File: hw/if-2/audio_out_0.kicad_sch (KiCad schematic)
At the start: 18 parts, among them U4 TL072

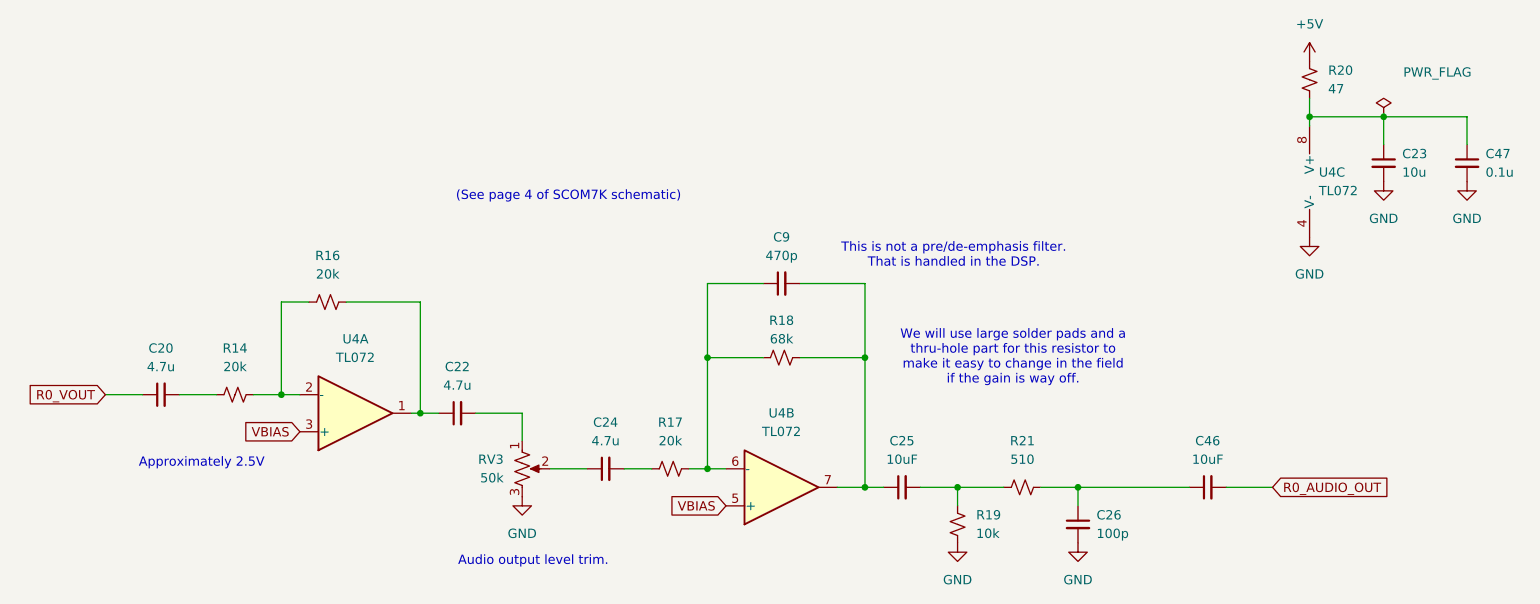
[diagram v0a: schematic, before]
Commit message: Ready to do layout on IF2 board
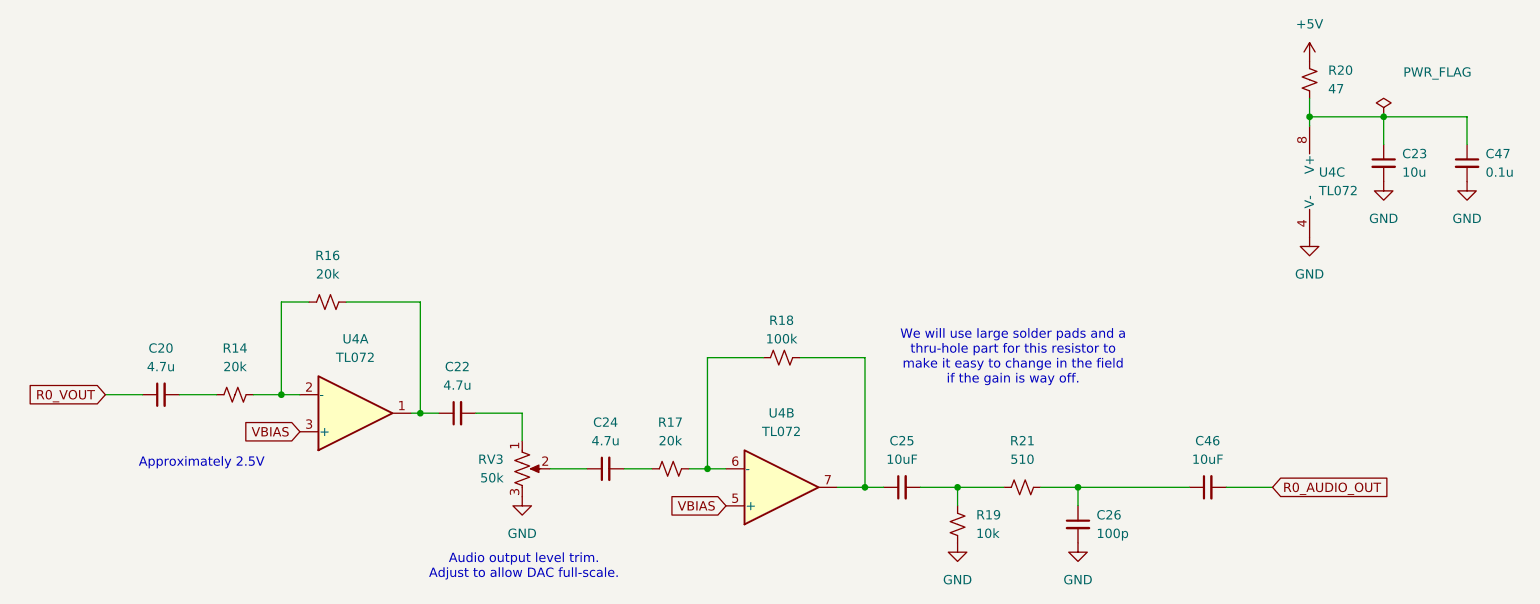
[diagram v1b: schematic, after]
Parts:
- removed C9: 470p, symbol Device:C_Small
- R18: value 68k -> 100k
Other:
- note added: "Audio output level trim. Adjust to allow DAC full-scale."
- note removed: "(See page 4 of SCOM7K schematic)"
- note removed: "Audio output level trim."
- note removed: "This is not a pre/de-emphasis filter. That is handled in the DSP."
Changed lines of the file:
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@@
 		)
 	)
-	(text "Audio output level trim.\n"
-		(exclude_from_sim no)
-		(at 122.174 96.52 0)
+	(text "Audio output level trim.\nAdjust to allow DAC full-scale.\n"
+		(exclude_from_sim no)
+		(at 120.904 97.282 0)
 		(effects
 			(font
 				(size 1.27 1.27)
-			)
-		)
-	)
-	(text "(See page 4 of SCOM7K schematic)"
-		(exclude_from_sim no)
-		(at 127 46.482 0)
-		(effects
-			(font
-				(size 1.27 1.27)
-			)
-		)
-	)
-	(text "This is not a pre/de-emphasis filter.\nThat is handled in the DSP."
-		(exclude_from_sim no)
-		(at 179.832 54.61 0)
-		(effects
-			(font
-				(size 1.27 1.27)
-				(color 255 4 2 1)
 			)
 		)
@@
 	)
 	(junction
-		(at 167.64 68.58)
-		(diameter 0)
-		(color 0 0 0 0)
-	)
-	(junction
 		(at 106.68 76.2)
 		(diameter 0)
@@
 	)
 	(junction
-		(at 146.05 68.58)
-		(diameter 0)
-		(color 0 0 0 0)
-	)
-	(junction
 		(at 238.76 35.56)
 		(diameter 0)
@@
 	(wire
 		(pts
-			(xy 167.64 58.42) (xy 167.64 68.58)
-		)
-		(stroke
-			(width 0)
-			(type default)
-		)
-	)
-	(wire
-		(pts
 			(xy 87.63 73.66) (xy 90.17 73.66)
 		)
@@
 	(wire
 		(pts
-			(xy 158.75 58.42) (xy 167.64 58.42)
-		)
-		(stroke
-			(width 0)
-			(type default)
-		)
-	)
-	(wire
-		(pts
 			(xy 228.6 35.56) (xy 228.6 36.83)
 		)
@@
 	(wire
 		(pts
-			(xy 146.05 58.42) (xy 146.05 68.58)
-		)
-		(stroke
-			(width 0)
-			(type default)
-		)
-	)
-	(wire
-		(pts
 			(xy 146.05 83.82) (xy 148.59 83.82)
 		)
@@
 		(pts
 			(xy 106.68 76.2) (xy 109.22 76.2)
-		)
-		(stroke
-			(width 0)
-			(type default)
-		)
-	)
-	(wire
-		(pts
-			(xy 153.67 58.42) (xy 146.05 58.42)
 		)
 		(stroke
@@
 	(symbol
 		(lib_id "Device:C_Small")
-		(at 156.21 58.42 90)
-		(unit 1)
-		(exclude_from_sim no)
-		(in_bom yes)
-		(on_board yes)
-		(dnp no)
-		(fields_autoplaced yes)
-		(property "Reference" "C9"
-			(at 156.2163 52.07 90)
-			(effects
-				(font
-					(size 1.27 1.27)
-				)
-			)
-		)
-		(property "Value" "470p"
-			(at 156.2163 54.61 90)
-			(effects
-				(font
-					(size 1.27 1.27)
-				)
-			)
-		)
-		(property "Footprint" ""
-			(at 156.21 58.42 0)
-			(effects
-				(font
-					(size 1.27 1.27)
-				)
-				(hide yes)
-			)
-		)
-		(property "Datasheet" "~"
-			(at 156.21 58.42 0)
-			(effects
-				(font
-					(size 1.27 1.27)
-				)
-				(hide yes)
-			)
-		)
-		(property "Description" "Unpolarized capacitor, small symbol"
-			(at 156.21 58.42 0)
-			(effects
-				(font
-					(size 1.27 1.27)
-				)
-				(hide yes)
-			)
-		)
-		(pin "1"
-		)
-		(pin "2"
-		)
-		(instances
-			(project ""
-				(path "/a8c2d6aa-29bb-49bd-a367-0d62a0a32480/44344ba6-1370-4a77-ab96-dbf60268a0b4"
-					(reference "C9")
-					(unit 1)
-				)
-			)
-		)
-	)
-	(symbol
-		(lib_id "Device:C_Small")
 		(at 172.72 86.36 90)
 		(unit 1)
@@
 			)
 		)
-		(property "Value" "68k"
+		(property "Value" "100k"
 			(at 156.21 66.04 90)
 			(effects

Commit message: Ready to do layout on IF2 board
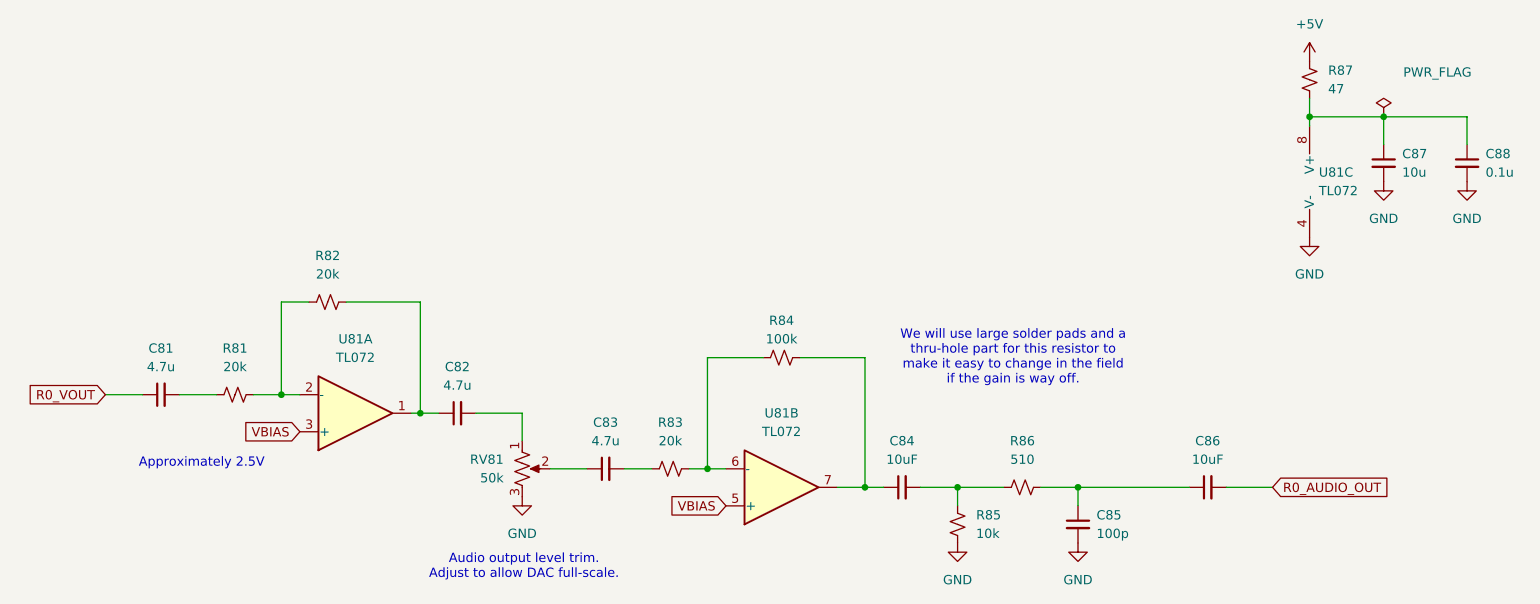
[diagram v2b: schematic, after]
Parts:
- R84: renamed from R18; footprint Resistor_SMD:R_0805_2012Metric_Pad1.20x1.40mm_HandSolder -> Resistor_THT:R_Axial_DIN0516_L15.5mm_D5.0mm_P5.08mm_Vertical
- U81: renamed from U4; footprint (none) -> Package_SO:SOIC-8_3.9x4.9mm_P1.27mm
- renumbered C20 to C81, C22 to C82, C24 to C83, C25 to C84, C26 to C85, C46 to C86, C23 to C87, C47 to C88, R14 to R81, R16 to R82, R17 to R83, R19 to R85, R21 to R86, R20 to R87, RV3 to RV81
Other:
- title: Audio Output Processing (Radio 0) -> COS/CTCSS/PTT Controls (Radio 1)
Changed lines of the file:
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@@
 	(paper "USLetter")
 	(title_block
-		(title "Audio Output Processing (Radio 0)")
+		(title "COS/CTCSS/PTT Controls (Radio 1)")
 		(date "2025-03-18")
 		(rev "2")
@@
 		(dnp no)
 		(fields_autoplaced yes)
-		(property "Reference" "#PWR067"
+		(property "Reference" "#PWR0138"
 			(at 196.85 100.33 0)
 			(effects
@@
 			(project "if-2"
 				(path "/a8c2d6aa-29bb-49bd-a367-0d62a0a32480/44344ba6-1370-4a77-ab96-dbf60268a0b4"
-					(reference "#PWR067")
+					(reference "#PWR0138")
 					(unit 1)
 				)
@@
 		(dnp no)
 		(fields_autoplaced yes)
-		(property "Reference" "C20"
+		(property "Reference" "C81"
 			(at 71.1263 67.31 90)
 			(effects
@@
 			(project "if-2"
 				(path "/a8c2d6aa-29bb-49bd-a367-0d62a0a32480/44344ba6-1370-4a77-ab96-dbf60268a0b4"
-					(reference "C20")
+					(reference "C81")
 					(unit 1)
 				)
@@
 		(dnp no)
 		(fields_autoplaced yes)
-		(property "Reference" "#PWR066"
+		(property "Reference" "#PWR0137"
 			(at 180.34 100.33 0)
 			(effects
@@
 			(project "if-2"
 				(path "/a8c2d6aa-29bb-49bd-a367-0d62a0a32480/44344ba6-1370-4a77-ab96-dbf60268a0b4"
-					(reference "#PWR066")
+					(reference "#PWR0137")
 					(unit 1)
 				)
@@
 		(dnp no)
 		(fields_autoplaced yes)
-		(property "Reference" "#PWR022"
+		(property "Reference" "#PWR0142"
 			(at 250.19 50.8 0)
 			(effects
@@
 			(project "if-2"
 				(path "/a8c2d6aa-29bb-49bd-a367-0d62a0a32480/44344ba6-1370-4a77-ab96-dbf60268a0b4"
-					(reference "#PWR022")
+					(reference "#PWR0142")
 					(unit 1)
 				)
@@
 		(dnp no)
 		(fields_autoplaced yes)
-		(property "Reference" "U4"
+		(property "Reference" "U81"
 			(at 229.87 43.1799 0)
 			(effects
@@
 			)
 		)
-		(property "Footprint" ""
+		(property "Footprint" "Package_SO:SOIC-8_3.9x4.9mm_P1.27mm"
 			(at 231.14 44.45 0)
 			(effects
@@
 			(project ""
 				(path "/a8c2d6aa-29bb-49bd-a367-0d62a0a32480/44344ba6-1370-4a77-ab96-dbf60268a0b4"
-					(reference "U4")
+					(reference "U81")
 					(unit 3)
 				)
@@
 		(dnp no)
 		(fields_autoplaced yes)
-		(property "Reference" "C23"
+		(property "Reference" "C87"
 			(at 241.3 40.6462 0)
 			(effects
@@
 			(project "if-2"
 				(path "/a8c2d6aa-29bb-49bd-a367-0d62a0a32480/44344ba6-1370-4a77-ab96-dbf60268a0b4"
-					(reference "C23")
+					(reference "C87")
 					(unit 1)
 				)
@@
 		(dnp no)
 		(fields_autoplaced yes)
-		(property "Reference" "RV3"
+		(property "Reference" "RV81"
 			(at 118.11 82.5499 0)
 			(effects
@@
 			(project "if-2"
 				(path "/a8c2d6aa-29bb-49bd-a367-0d62a0a32480/44344ba6-1370-4a77-ab96-dbf60268a0b4"
-					(reference "RV3")
+					(reference "RV81")
 					(unit 1)
 				)
@@
 		(dnp no)
 		(fields_autoplaced yes)
-		(property "Reference" "R16"
+		(property "Reference" "R82"
 			(at 93.98 54.61 90)
 			(effects
@@
 			(project "if-2"
 				(path "/a8c2d6aa-29bb-49bd-a367-0d62a0a32480/44344ba6-1370-4a77-ab96-dbf60268a0b4"
-					(reference "R16")
+					(reference "R82")
 					(unit 1)
 				)
@@
 		(dnp no)
 		(fields_autoplaced yes)
-		(property "Reference" "#PWR019"
+		(property "Reference" "#PWR0140"
 			(at 228.6 58.42 0)
 			(effects
@@
 			(project "if-2"
 				(path "/a8c2d6aa-29bb-49bd-a367-0d62a0a32480/44344ba6-1370-4a77-ab96-dbf60268a0b4"
-					(reference "#PWR019")
+					(reference "#PWR0140")
 					(unit 1)
 				)
@@
 		(dnp no)
 		(fields_autoplaced yes)
-		(property "Reference" "R14"
+		(property "Reference" "R81"
 			(at 81.28 67.31 90)
 			(effects
@@
 			(project "if-2"
 				(path "/a8c2d6aa-29bb-49bd-a367-0d62a0a32480/44344ba6-1370-4a77-ab96-dbf60268a0b4"
-					(reference "R14")
+					(reference "R81")
 					(unit 1)
 				)
@@
 		(dnp no)
 		(fields_autoplaced yes)
-		(property "Reference" "R19"
+		(property "Reference" "R85"
 			(at 182.88 90.1699 0)
 			(effects
@@
 			(project "if-2"
 				(path "/a8c2d6aa-29bb-49bd-a367-0d62a0a32480/44344ba6-1370-4a77-ab96-dbf60268a0b4"
-					(reference "R19")
+					(reference "R85")
 					(unit 1)
 				)
@@
 		(dnp no)
 		(fields_autoplaced yes)
-		(property "Reference" "U4"
+		(property "Reference" "U81"
 			(at 156.21 76.2 0)
 			(effects
@@
 			)
 		)
-		(property "Footprint" ""
+		(property "Footprint" "Package_SO:SOIC-8_3.9x4.9mm_P1.27mm"
 			(at 156.21 86.36 0)
 			(effects
@@
 			(project ""
 				(path "/a8c2d6aa-29bb-49bd-a367-0d62a0a32480/44344ba6-1370-4a77-ab96-dbf60268a0b4"
-					(reference "U4")
+					(reference "U81")
 					(unit 2)
 				)
@@
 		(dnp no)
 		(fields_autoplaced yes)
-		(property "Reference" "R21"
+		(property "Reference" "R86"
 			(at 189.23 80.01 90)
 			(effects
@@
 			(project "if-2"
 				(path "/a8c2d6aa-29bb-49bd-a367-0d62a0a32480/44344ba6-1370-4a77-ab96-dbf60268a0b4"
-					(reference "R21")
+					(reference "R86")
 					(unit 1)
 				)
@@
 		(dnp no)
 		(fields_autoplaced yes)
-		(property "Reference" "R17"
+		(property "Reference" "R83"
 			(at 140.97 77.47 90)
 			(effects
@@
 			(project "if-2"
 				(path "/a8c2d6aa-29bb-49bd-a367-0d62a0a32480/44344ba6-1370-4a77-ab96-dbf60268a0b4"
-					(reference "R17")
+					(reference "R83")
 					(unit 1)
 				)
@@
 		(on_board yes)
 		(dnp no)
-		(property "Reference" "#FLG011"
+		(property "Reference" "#FLG081"
 			(at 238.76 33.655 0)
 			(effects
@@
 			(project "if-2"
 				(path "/a8c2d6aa-29bb-49bd-a367-0d62a0a32480/44344ba6-1370-4a77-ab96-dbf60268a0b4"
-					(reference "#FLG011")
+					(reference "#FLG081")
 					(unit 1)
 				)
@@
 		(dnp no)
 		(fields_autoplaced yes)
-		(property "Reference" "C25"
+		(property "Reference" "C84"
 			(at 172.7263 80.01 90)
 			(effects
@@
 			(project "if-2"
 				(path "/a8c2d6aa-29bb-49bd-a367-0d62a0a32480/44344ba6-1370-4a77-ab96-dbf60268a0b4"
-					(reference "C25")
+					(reference "C84")
 					(unit 1)
 				)
@@
 		(dnp no)
 		(fields_autoplaced yes)
-		(property "Reference" "C46"
+		(property "Reference" "C86"
 			(at 214.6363 80.01 90)
 			(effects
@@
 			(project "if-2"
 				(path "/a8c2d6aa-29bb-49bd-a367-0d62a0a32480/44344ba6-1370-4a77-ab96-dbf60268a0b4"
-					(reference "C46")
+					(reference "C86")
 					(unit 1)
 				)
@@
 		(dnp no)
 		(fields_autoplaced yes)
-		(property "Reference" "U4"
+		(property "Reference" "U81"
 			(at 97.79 66.04 0)
 			(effects
@@
 			)
 		)
-		(property "Footprint" ""
+		(property "Footprint" "Package_SO:SOIC-8_3.9x4.9mm_P1.27mm"
 			(at 97.79 76.2 0)
 			(effects
@@
 			(project ""
 				(path "/a8c2d6aa-29bb-49bd-a367-0d62a0a32480/44344ba6-1370-4a77-ab96-dbf60268a0b4"
-					(reference "U4")
+					(reference "U81")
 					(unit 1)
 				)
@@
 		(dnp no)
 		(fields_autoplaced yes)
-		(property "Reference" "C24"
+		(property "Reference" "C83"
 			(at 132.0863 77.47 90)
 			(effects
@@
 			(project "if-2"
 				(path "/a8c2d6aa-29bb-49bd-a367-0d62a0a32480/44344ba6-1370-4a77-ab96-dbf60268a0b4"
-					(reference "C24")
+					(reference "C83")
 					(unit 1)
 				)
@@
 		(dnp no)
 		(fields_autoplaced yes)
-		(property "Reference" "R20"
+		(property "Reference" "R87"
 			(at 231.14 29.2099 0)
 			(effects
@@
 			(project "if-2"
 				(path "/a8c2d6aa-29bb-49bd-a367-0d62a0a32480/44344ba6-1370-4a77-ab96-dbf60268a0b4"
-					(reference "R20")
+					(reference "R87")
 					(unit 1)
 				)
@@
 		(dnp no)
 		(fields_autoplaced yes)
-		(property "Reference" "C26"
+		(property "Reference" "C85"
 			(at 199.39 90.1762 0)
 			(effects
@@
 			(project "if-2"
 				(path "/a8c2d6aa-29bb-49bd-a367-0d62a0a32480/44344ba6-1370-4a77-ab96-dbf60268a0b4"
-					(reference "C26")
+					(reference "C85")
 					(unit 1)
 				)
@@
 		(dnp no)
 		(fields_autoplaced yes)
-		(property "Reference" "#PWR018"
+		(property "Reference" "#PWR0136"
 			(at 120.65 93.98 0)
 			(effects
@@
 			(project "if-2"
 				(path "/a8c2d6aa-29bb-49bd-a367-0d62a0a32480/44344ba6-1370-4a77-ab96-dbf60268a0b4"
-					(reference "#PWR018")
+					(reference "#PWR0136")
 					(unit 1)
 				)
@@
 		(on_board yes)
 		(dnp no)
-		(property "Reference" "R18"
+		(property "Reference" "R84"
 			(at 156.21 63.5 90)
 			(effects
@@
 			)
 		)
-		(property "Footprint" "Resistor_SMD:R_0805_2012Metric_Pad1.20x1.40mm_HandSolder"
+		(property "Footprint" "Resistor_THT:R_Axial_DIN0516_L15.5mm_D5.0mm_P5.08mm_Vertical"
 			(at 156.21 68.58 0)
 			(effects
@@
 			(project "if-2"
 				(path "/a8c2d6aa-29bb-49bd-a367-0d62a0a32480/44344ba6-1370-4a77-ab96-dbf60268a0b4"
-					(reference "R18")
+					(reference "R84")
 					(unit 1)
 				)
@@
 		(dnp no)
 		(fields_autoplaced yes)
-		(property "Reference" "#PWR021"
+		(property "Reference" "#PWR0141"
 			(at 238.76 50.8 0)
 			(effects
@@
 			(project "if-2"
 				(path "/a8c2d6aa-29bb-49bd-a367-0d62a0a32480/44344ba6-1370-4a77-ab96-dbf60268a0b4"
-					(reference "#PWR021")
+					(reference "#PWR0141")
 					(unit 1)
 				)
@@
 		(dnp no)
 		(fields_autoplaced yes)
-		(property "Reference" "C22"
+		(property "Reference" "C82"
 			(at 111.7663 69.85 90)
 			(effects
@@
 			(project "if-2"
 				(path "/a8c2d6aa-29bb-49bd-a367-0d62a0a32480/44344ba6-1370-4a77-ab96-dbf60268a0b4"
-					(reference "C22")
+					(reference "C82")
 					(unit 1)
 				)
@@
 		(dnp no)
 		(fields_autoplaced yes)
-		(property "Reference" "C47"
+		(property "Reference" "C88"
 			(at 252.73 40.6462 0)
 			(effects
@@
 			(project "if-2"
 				(path "/a8c2d6aa-29bb-49bd-a367-0d62a0a32480/44344ba6-1370-4a77-ab96-dbf60268a0b4"
-					(reference "C47")
+					(reference "C88")
 					(unit 1)
 				)
@@
 		(dnp no)
 		(fields_autoplaced yes)
-		(property "Reference" "#PWR020"
+		(property "Reference" "#PWR0139"
 			(at 228.6 31.75 0)
 			(effects
@@
 			(project "if-2"
 				(path "/a8c2d6aa-29bb-49bd-a367-0d62a0a32480/44344ba6-1370-4a77-ab96-dbf60268a0b4"
-					(reference "#PWR020")
-					(unit 1)
-				)
+					(reference "#PWR0139")
+					(unit 1)
+				)

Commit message: Making progress on layout
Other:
- title: COS/CTCSS/PTT Controls (Radio 1) -> COS/CTCSS/PTT Controls (Radio 0)
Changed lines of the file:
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@@
 	(paper "USLetter")
 	(title_block
-		(title "COS/CTCSS/PTT Controls (Radio 1)")
-		(date "2025-03-18")
+		(title "COS/CTCSS/PTT Controls (Radio 0)")
+		(date "2025-05-09")
 		(rev "2")
 		(company "Bruce MacKinnon KC1FSZ")

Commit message: Making progress on layout
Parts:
- added TP6: TestPoint, TestPoint:TestPoint_Pad_2.5x2.5mm, symbol Connector:TestPoint
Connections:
- net R0_VOUT: now also TP6.1
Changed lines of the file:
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@@
+	)
+	(junction
+		(at 67.31 73.66)
+		(diameter 0)
+		(color 0 0 0 0)
 	)
 	(junction
@@
 	(wire
 		(pts
+			(xy 67.31 66.04) (xy 67.31 73.66)
+		)
+		(stroke
+			(width 0)
+			(type default)
+		)
+	)
+	(wire
+		(pts
 			(xy 134.62 83.82) (xy 138.43 83.82)
 		)
@@
 	(wire
 		(pts
-			(xy 63.5 73.66) (xy 68.58 73.66)
+			(xy 63.5 73.66) (xy 67.31 73.66)
 		)
 		(stroke
@@
 		(pts
 			(xy 106.68 60.96) (xy 106.68 76.2)
+		)
+		(stroke
+			(width 0)
+			(type default)
+		)
+	)
+	(wire
+		(pts
+			(xy 67.31 73.66) (xy 68.58 73.66)
 		)
 		(stroke
@@
 				)
 			)
+		)
+	)
+	(symbol
+		(lib_id "Connector:TestPoint")
+		(at 67.31 66.04 0)
+		(unit 1)
+		(exclude_from_sim no)
+		(in_bom yes)
+		(on_board yes)
+		(dnp no)
+		(fields_autoplaced yes)
+		(property "Reference" "TP6"
+			(at 69.85 61.4679 0)
+			(effects
+				(font
+					(size 1.27 1.27)
+				)
+				(justify left)
+			)
+		)
+		(property "Value" "TestPoint"
+			(at 69.85 64.0079 0)
+			(effects
+				(font
+					(size 1.27 1.27)
+				)
+				(justify left)
+			)
+		)
+		(property "Footprint" "TestPoint:TestPoint_Pad_2.5x2.5mm"
+			(at 72.39 66.04 0)
+			(effects
+				(font
+					(size 1.27 1.27)
+				)
+				(hide yes)
+			)
+		)
+		(property "Datasheet" "~"
+			(at 72.39 66.04 0)
+			(effects
+				(font
+					(size 1.27 1.27)
+				)
+				(hide yes)
+			)
+		)
+		(property "Description" "test point"
+			(at 67.31 66.04 0)
+			(effects
+				(font
+					(size 1.27 1.27)
+				)
+				(hide yes)
+			)
+		)
+		(pin "1"
+		)
+		(instances
+			(project "if-2"
+				(path "/a8c2d6aa-29bb-49bd-a367-0d62a0a32480/44344ba6-1370-4a77-ab96-dbf60268a0b4"
+					(reference "TP6")
+					(unit 1)
+				)
+			)
